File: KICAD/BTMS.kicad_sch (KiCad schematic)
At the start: 154 parts, among them J1 Batt_Ballance, J2 AUX_Charge, J3 Battery_IO, J4 Power_Out, J5 BT_LM62, J6 DSKY, J7 PWR_SW, J8 ICSP, J9 Heater, P1 USB_C_Plug, Q1 SSM3K341R, Q2 DMN65D8L, Q3 SSM3K341R, Q4 FDN340P, Q5 FDN340P, Q6 FDN340P, Q7 DMN65D8L, Q8 DMN65D8L, SW1 PTS526, U1 ACS711xLCTR-25AB, U10 BA033CC0FP-E2, U11 AON7522E, U12 AON7522E, U13 LM62CIM3/NOPB, U14 FAN3100TSX, U15 FAN3100TSX, U16 AON7522E, U17 dsPIC30F3011-PT, U18 FT230XQ, U2 AP33771, U3 IS281-4, U4 Q294700DSGR, U5 SCF4030-12-0X, U6 AONR21321, U7 ACS711xLCTR-25AB, U8 IS281-4, U9 IRS2184

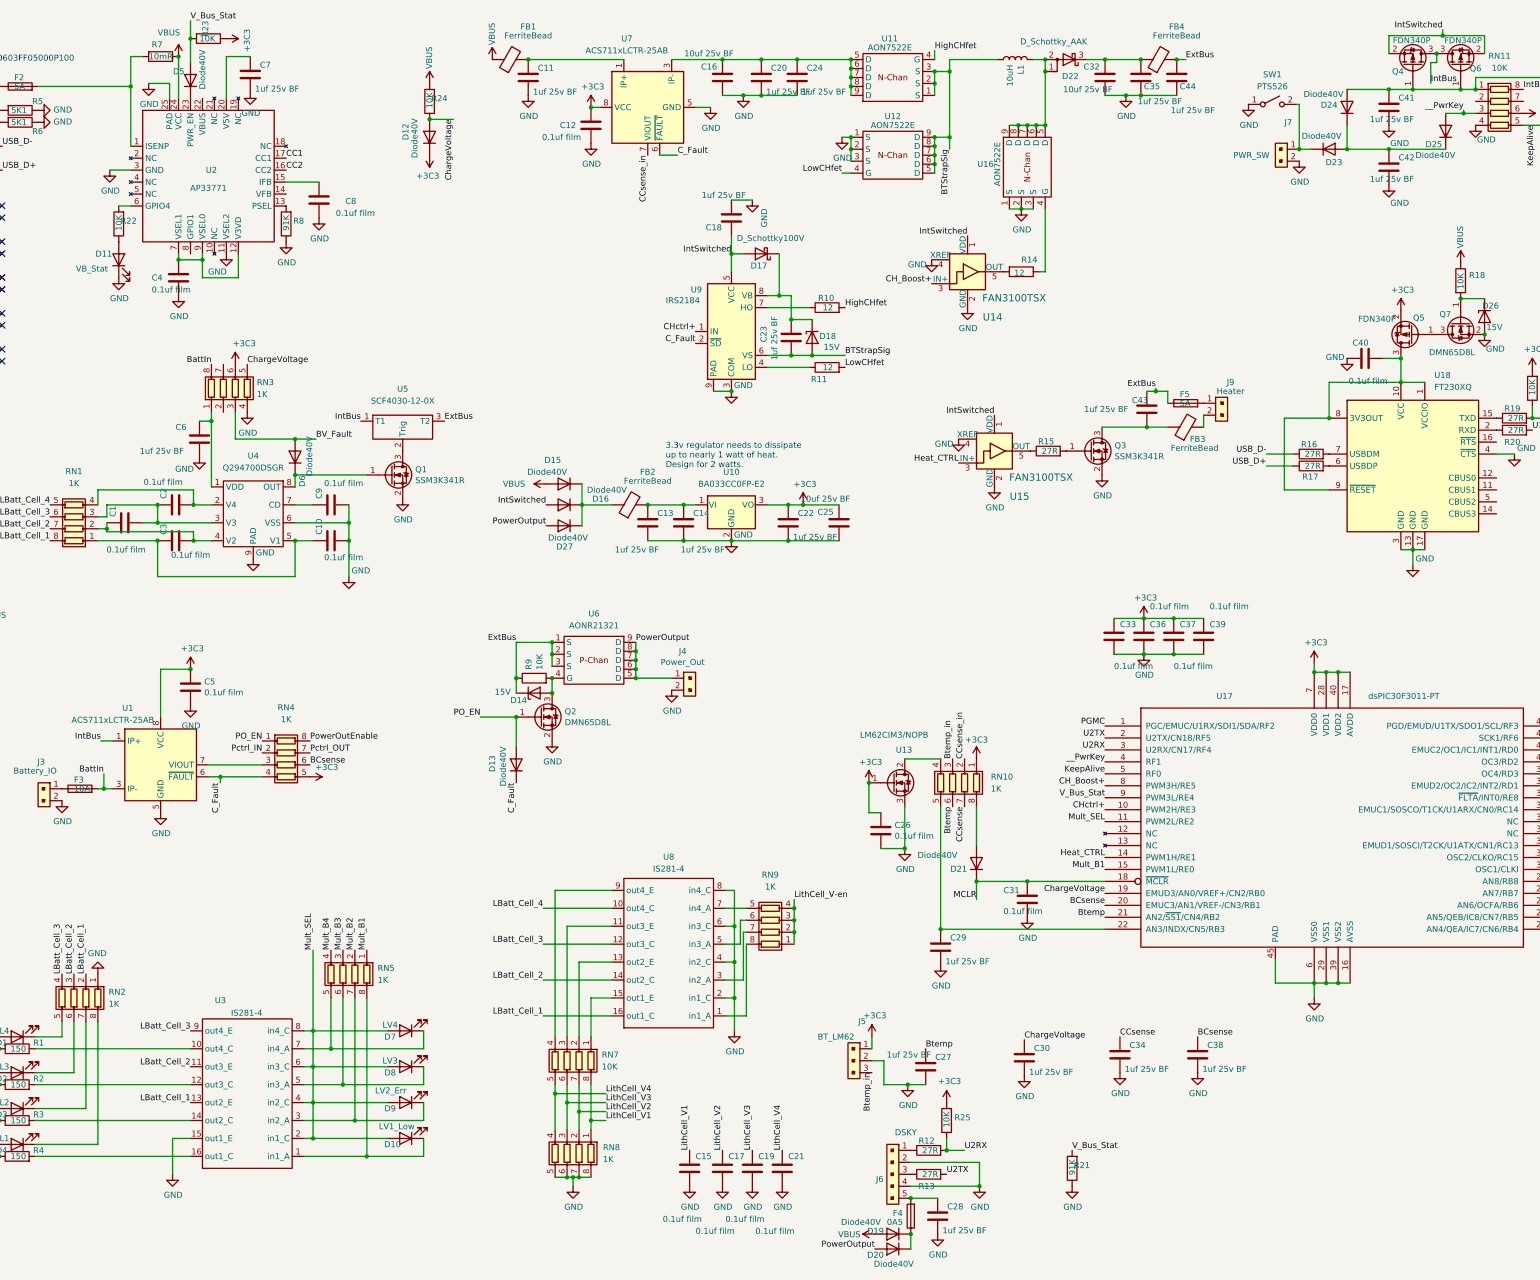
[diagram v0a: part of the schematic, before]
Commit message: Cleaned up some things. Price optimized capacitors.
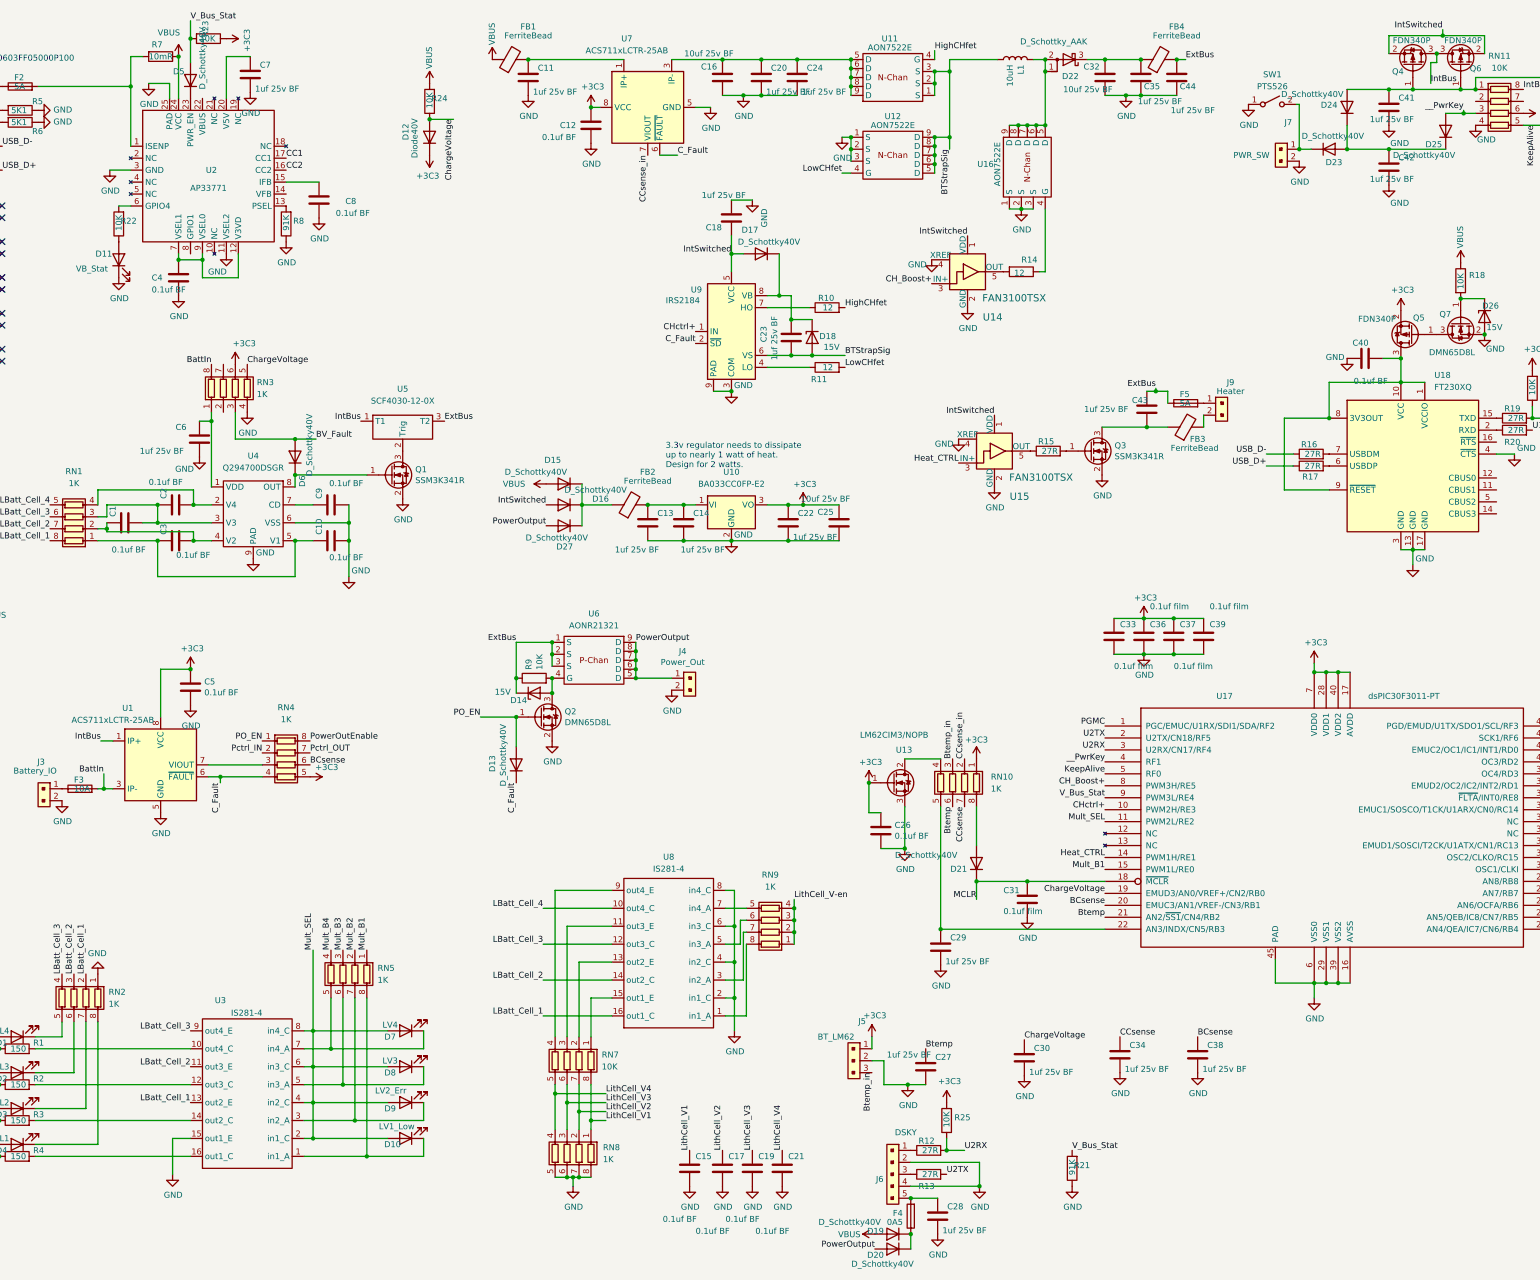
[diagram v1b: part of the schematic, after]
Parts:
- removed D17: D_Schottky100V, Diode_SMD:D_SOD-123, symbol Device:D_Schottky
- added D17: D_Schottky40V, Diode_SMD:D_0603_1608Metric, symbol Device:D
- C1, C10, C12, C15, C17, C19, C2, C21, C26, C3, C4, C40, C5, C8, C9: value 0.1uf film -> 0.1uf BF; DK_Detail_Page https://www.digikey.com/en/products/detail/panasonic-electr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 -> https://www.digikey.com/en/products/detail/kyocera-avx/KGF1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; Digi-Key_PN PCF1126CT-ND -> 478-KGF15AR71H104KTCT-ND
- D13, D15, D16, D19, D20, D21, D23, D24, D25, D27, D5, D6: value Diode40V -> D_Schottky40V
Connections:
- net IntSwitched: now also D17.2 (A)
- net at C23.1, D18.1 (K), U9.8 (VB): now also D17.1 (K)

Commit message: Removed unneeded 15V zener diodes. Added pre-charge circuit to output to reduce inrush current. Removed power control circuit from FTDI chip. Fixed USB-C connector.
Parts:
- removed D14, D18, D26: 15V, Diode_SMD:D_SOD-123, symbol Device:D_Zener
- removed P1: USB_C_Plug, Connector_USB:USB_C_Receptacle_GCT_USB4085, symbol Connector:USB_C_Plug
- removed Q5: FDN340P, Package_TO_SOT_SMD:SOT-23, symbol Device:Q_PMOS_GSD
- removed Q7: DMN65D8L, Package_TO_SOT_SMD:SOT-23, symbol Device:Q_NMOS_GSD
- removed R18: 10K, Resistor_SMD:R_0603_1608Metric, symbol Device:R
- added C45: 10uf 25v BF, Capacitor_SMD:C_0805_2012Metric, symbol Device:C
- added D28: D_Schottky40V, Diode_SMD:D_0603_1608Metric, symbol Device:D
- added J10: USB_C_Receptacle_4085, Connector_USB:USB_C_Receptacle_GCT_USB4085, symbol Connector:USB_C_Receptacle
- added Q10: DMN65D8L, Package_TO_SOT_SMD:SOT-23, symbol Device:Q_NMOS_GSD
- added Q11, Q9: FDN340P, Package_TO_SOT_SMD:SOT-23, symbol Device:Q_PMOS_GSD
- added R27, R28, R29: 10K, Resistor_SMD:R_0603_1608Metric, symbol Device:R
- added R30: 150, Resistor_SMD:R_0805_2012Metric_Pad1.20x1.40mm_HandSolder, symbol Device:R
- C43: value 1uf 25v BF -> 0.1uf BF; DK_Detail_Page https://www.digikey.com/en/products/detail/tdk-corporation/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 -> https://www.digikey.com/en/products/detail/kyocera-avx/KGF1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; Digi-Key_PN 445-173615-1-ND -> 478-KGF15AR71H104KTCT-ND
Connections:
- net +5C: now also C40.2, RN9.1 (R1.1), RN9.2 (R2.1), RN9.3 (R3.1), RN9.4 (R4.1), U18.1 (VCCIO), U18.10 (VCC), U18.8 (3V3OUT), U18.9 (~{RESET}), Q9.2 (S)
- net CC1: now also J10.A5 (CC1)
- net CC2: now also J10.B5 (CC2)
- net C_Fault: now also D28.1 (K), Q9.1 (G); no longer U17.42 (EMUC2/OC1/IC1/INT1/RD0)
- net ExtBus: now also C45.1, Q11.2 (S), R29.1
- net GND: now also C45.2, J10.A1 (GND), J10.A12 (GND), J10.B1 (GND), J10.B12 (GND), J10.S1 (SHIELD), Q10.2 (S), R27.1
- net PO_EN: now also D28.2 (A); no longer D13.2 (A)
- net PowerOutput: now also R30.2
- net USB_D+: now also J10.A6 (D+), J10.B6 (D+)
- net USB_D-: now also J10.A7 (D-), J10.B7 (D-)
- net at F2.1: now also J10.A4 (VBUS), J10.A9 (VBUS), J10.B4 (VBUS), J10.B9 (VBUS)
- removed net LithCell_V-en: RN9.1 (R1.1), RN9.2 (R2.1), RN9.3 (R3.1), RN9.4 (R4.1), U17.43 (SCK1/RF6)
- new net: D13.2 (A), Q10.1 (G), R28.2
- new net: Q10.3 (D), Q11.1 (G), R29.2
- new net: Q11.3 (D), R30.1
- new net C_Fault_In: Q9.3 (D), R27.2, U17.42 (EMUC2/OC1/IC1/INT1/RD0)
- new net Pre_Charge: R28.1, U17.43 (SCK1/RF6)
- no-connect marks 10 -> 2
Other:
- note removed: "MFU0603FF05000P100"
- note removed: "USB-C Connector"
- moved on the sheet: D13, J4, Q2, R9, U6

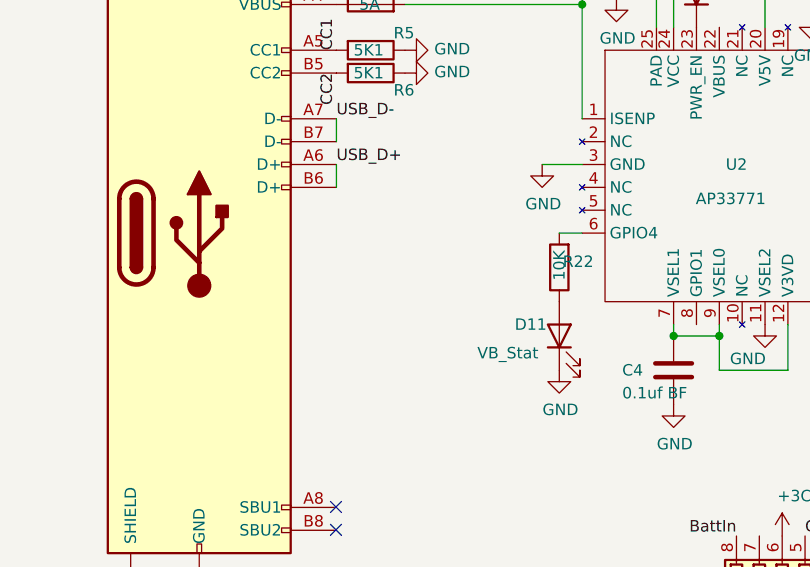
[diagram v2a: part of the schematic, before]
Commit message: Fixed chip resistor array footprints. <- Need to finish re-routing traces and update G-Code files.
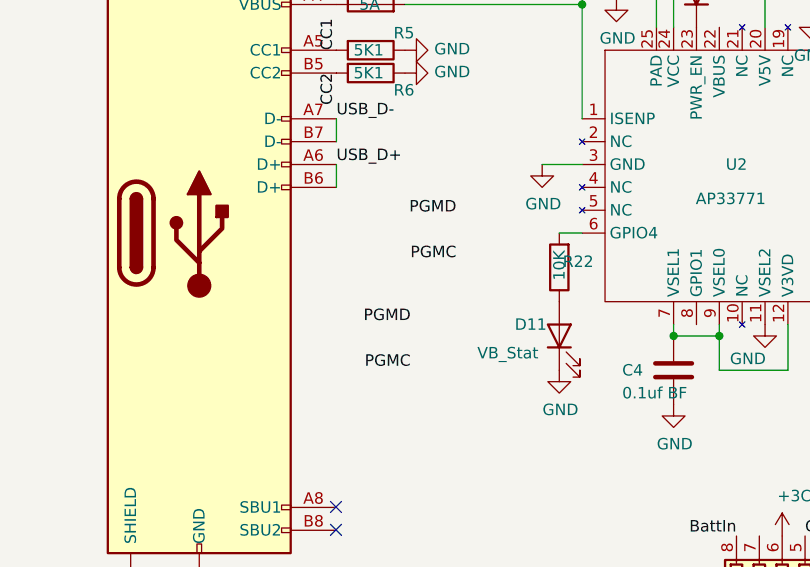
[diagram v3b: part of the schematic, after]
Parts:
- RN1, RN10, RN11, RN2, RN3, RN4, RN5, RN7, RN8, RN9: footprint Resistor_SMD:R_Array_Convex_4x1206 -> Resistor_SMD:R_Array_Convex_4x0612
- U11, U12, U16: footprint Package_DFN_QFN:DFN-8-1EP_3x3mm_P0.5mm_EP1.65x2.38mm_ThermalVias -> Package_DFN_QFN:DFN-8-1EP_3x3mm_P0.65mm_EP1.7x2.05mm
- U6: footprint Package_DFN_QFN:DFN-8-1EP_3x3mm_P0.5mm_EP1.65x2.38mm -> Package_DFN_QFN:DFN-8-1EP_3x3mm_P0.65mm_EP1.7x2.05mm

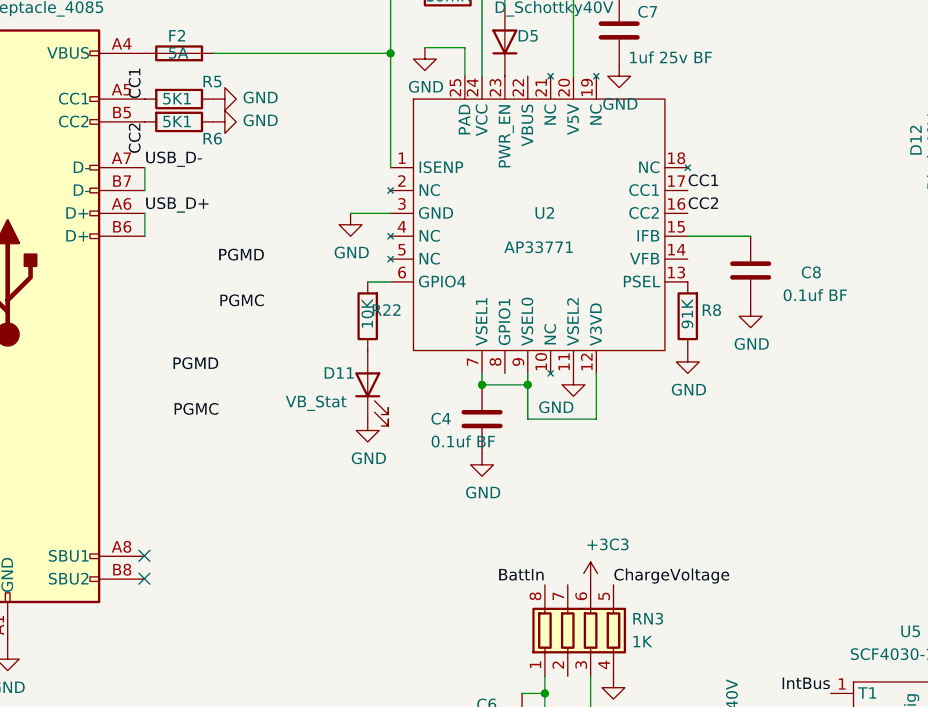
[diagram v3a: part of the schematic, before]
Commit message: Finished routing for fixed resistor array footprints. Added I2C lines to USB-3 PD chip to dsPIC. Cleaned up ground-plane islands and tails.
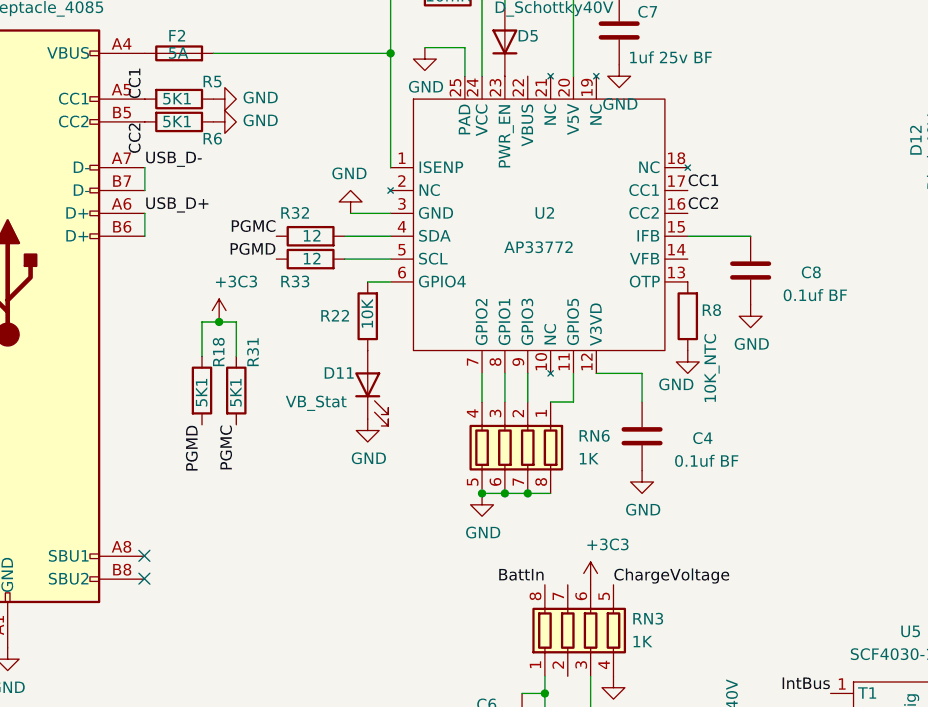
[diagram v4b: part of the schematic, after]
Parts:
- added R18, R31: 5K1, Resistor_SMD:R_0603_1608Metric, symbol Device:R
- added R32, R33: 12, Resistor_SMD:R_0603_1608Metric, symbol Device:R
- added RN6: 1K, Resistor_SMD:R_Array_Convex_4x0612, symbol Device:R_Pack04
- R8: value 91K -> 10K_NTC
- U2: value AP33771 -> AP33772
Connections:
- net +5C: now also R18.1, R31.1
- net GND: now also RN6.5 (R4.2), RN6.6 (R3.2), RN6.7 (R2.2), RN6.8 (R1.2); no longer U2.11 (VSEL2)
- net PGMC: now also R31.2, R32.1
- net PGMD: now also R18.2, R33.1
- net at C4.1, U2.12 (V3VD): no longer U2.7 (VSEL1), U2.9 (VSEL0)
- net at U2.4 (SDA): now also R32.2
- net at U2.5 (SCL): now also R33.2
- net at U2.8 (GPIO1): now also RN6.3 (R3.1)
- new net: RN6.1 (R1.1), U2.11 (GPIO5)
- new net: RN6.2 (R2.1), U2.9 (GPIO3)
- new net: RN6.4 (R4.1), U2.7 (GPIO2)

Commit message: Began expirimenting with clock switching to reduce power draw. Managed to double idle runtime. Started runtime calculations. Fixed some things in schematic.
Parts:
- removed C15, C17, C19, C21: 0.1uf BF, Capacitor_SMD:C_0603_1608Metric, symbol Device:C
- removed C31, C33, C36, C37, C39: 0.1uf film, Capacitor_SMD:C_0603_1608Metric, symbol Device:C
- removed FB2: FerriteBead, Resistor_SMD:R_1206_3216Metric, symbol Device:FerriteBead
- removed J5: BT_LM62, Connector_PinHeader_2.54mm:PinHeader_1x03_P2.54mm_Vertical, symbol BTMS-rescue:640456-3-dk_Rectangular-Connectors-Headers-Male-Pins
- removed R28: 10K, Resistor_SMD:R_0603_1608Metric, symbol Device:R
- removed RN3, RN8: 1K, Resistor_SMD:R_Array_Convex_4x0612, symbol Device:R_Pack04
- removed RN7: 10K, Resistor_SMD:R_Array_Convex_4x0612, symbol Device:R_Pack04
- removed U10: BA033CC0FP-E2, Package_TO_SOT_SMD:TO-252-2, symbol Regulator_Linear:LF33_TO252
- added C? (x3): 10uf 25v BF, Capacitor_SMD:C_0805_2012Metric, symbol Device:C
- added C? (x8): 0.1uf BF, Capacitor_SMD:C_0603_1608Metric, symbol Device:C
- added C? (x7): 1uf 25v BF, Capacitor_SMD:C_0603_1608Metric, symbol Device:C
- added J?: BatteryPTC, Connector_PinHeader_2.54mm:PinHeader_1x02_P2.54mm_Vertical, symbol BTMS-rescue:22-23-2021-dk_Rectangular-Connectors-Headers-Male-Pins
- added R? (x3): 10K, Resistor_SMD:R_0603_1608Metric, symbol Device:R
- added R?: 150, Resistor_SMD:R_0805_2012Metric_Pad1.20x1.40mm_HandSolder, symbol Device:R
- added R? (x2): 100, Resistor_SMD:R_0603_1608Metric, symbol Device:R
- added R?: 1K, Resistor_SMD:R_0603_1608Metric, symbol Device:R
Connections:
- net +5C: now also R24.2, U17.29 (VDD), U17.8 (VDD), C?.1, C?.1, C?.1, C?.1, C?.1, C?.1, C?.1; no longer C22.1, C25.1, U17.17 (AVDD)
- net BV_Fault: now also R24.1
- net BattIn: now also R?.2
- net Btemp: no longer C27.1
- net Btemp_in: now also C27.1, J?.2, R?.1
- net CH_Boost+: now also U17.9 (PWM3H/RE5); no longer U17.8 (PWM3H/RE5)
- net CHctrl+: now also U17.11 (PWM2H/RE3); no longer U17.10 (PWM2H/RE3)
- net ChargeVoltage: no longer R24.1
- net GND: now also U17.30 (VSS), U17.31 (VSS), C?.2, C?.2, C?.2, C?.2, C?.2, C?.2, C?.2, C?.2, C?.2, C?.2, C?.2, C?.2, C?.2, C?.2, C?.2, C?.2, C?.2, C?.2, J?.1, R?.1, R?.2; no longer RN2.1 (R1.1), U17.29 (VSS1)
- net LBatt_Cell_1: no longer RN2.2 (R2.1)
- net LBatt_Cell_2: no longer RN2.3 (R3.1)
- net LBatt_Cell_3: no longer RN2.4 (R4.1)
- net LithCell_V1: now also C?.1
- net LithCell_V2: now also C?.1
- net LithCell_V3: now also C?.1
- net LithCell_V4: now also C?.1
- net MCLR: now also R?.2; no longer D21.1 (K), U17.18 (~{MCLR})
- net Mult_SEL: now also U17.12 (PWM2L/RE2); no longer U17.11 (PWM2L/RE2)
- net PO_EN: now also R?.2
- net PowerOutEnable: now also U17.33 (OSC2/CLKO/RC15); no longer U17.31 (OSC2/CLKO/RC15)
- net PowerOutput: now also R?.2; no longer R30.2
- net Pre_Charge: now also R?.2
- net U1TX: now also U17.34 (EMUD1/SOSCI/T2CK/U1ATX/CN1/RC13); no longer U17.32 (EMUD1/SOSCI/T2CK/U1ATX/CN1/RC13)
- net VBUS: no longer R24.2
- net V_Bus_Stat: now also U17.10 (PWM3L/RE4); no longer U17.9 (PWM3L/RE4)
- net at C13.1, C14.1: now also C?.1
- net at D13.2 (A), Q10.1 (G): now also R?.1, R?.1
- net at C6.1, U4.1 (VDD): now also R?.1
- net at R1.2, U3.10 (out4_C): now also RN2.4 (R4.1)
- net at R2.2, U3.12 (out3_C): now also RN2.3 (R3.1)
- net at R3.2, U3.14 (out2_C): now also RN2.2 (R2.1)
- net at R4.2, U3.16 (out1_C): now also RN2.1 (R1.1)
- new net: C?.1, D21.1 (K), R?.1, U17.18 (~{MCLR})
- new net: C?.1, C?.1, C?.1
- new net: R30.2, R?.1
- new net +3.3VA: C22.1, C25.1, C?.1, C?.1, R?.2, U17.17 (AVDD)
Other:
- note added: "Using digital 3.3v instead of analog for this temperature sensor because it's not super ciritial how accurate it is, and this power line runs accross the board and could pickup noise."
- note removed: "3.3v regulator needs to dissipate up to nearly 1 watt of heat. Design for 2 watts."
- moved on the sheet: C1, C10, C11, C12, C13, C14, C16, C18, C2, C20, C22, C23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
